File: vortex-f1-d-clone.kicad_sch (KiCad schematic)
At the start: 60 parts, among them IC1 74LS136, IC10 uPD765AC, IC11 74LS01, IC12 74LS38, IC13 74LS07, IC14 74LS139, IC2 74LS74, IC3 74LS85, IC4 27128, IC5 74LS14, IC6 74LS08, IC7 74LS25, IC8 74LS32, IC9 FDC_9229

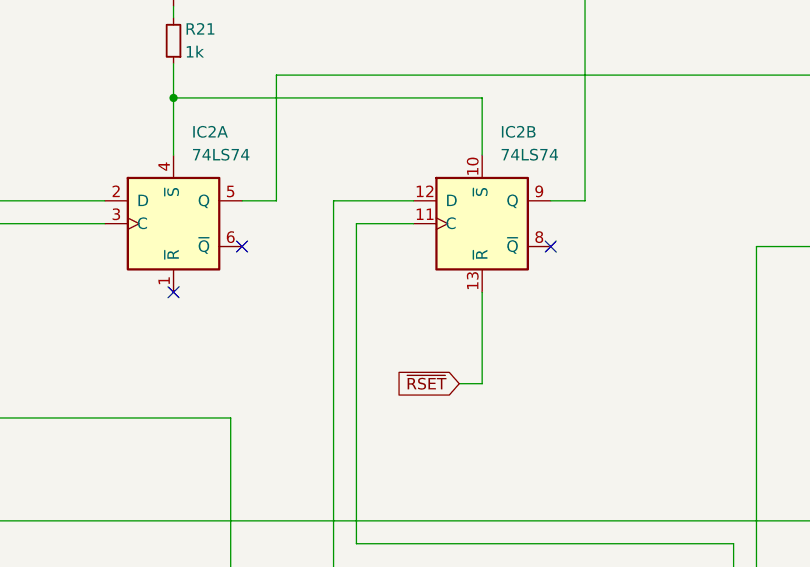
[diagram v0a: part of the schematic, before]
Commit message: Layout with ROM redone
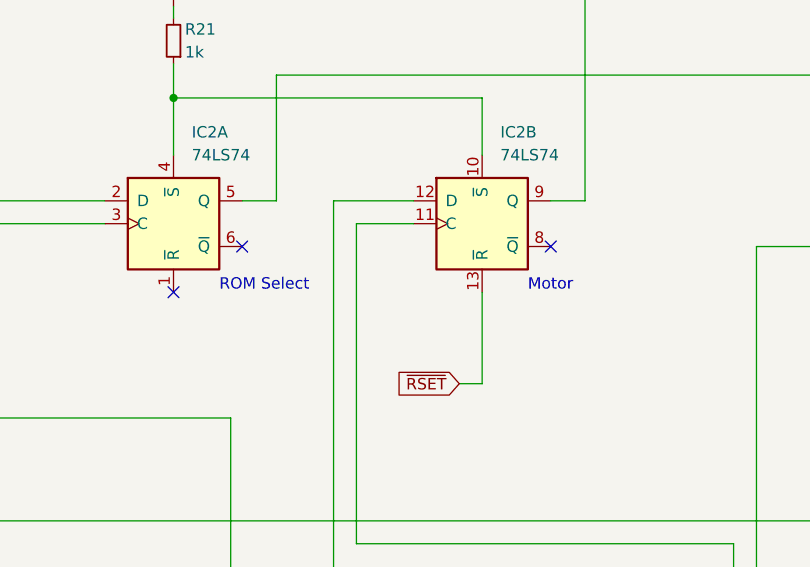
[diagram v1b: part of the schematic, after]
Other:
- note added: "Motor"
- note added: "ROM Select"
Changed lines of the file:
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@@
     (stroke (width 0) (type default) (color 0 0 0 0))
+  )
+  (text "Motor" (at 102.87 160.02 0)
+    (effects (font (size 1.27 1.27)) (justify left bottom))
+  )
+  (text "ROM Select\n" (at 68.58 160.02 0)
+    (effects (font (size 1.27 1.27)) (justify left bottom))
   )
   (label "D3" (at 63.5 297.18 0)

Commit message: sent TTL variant to aisler for production
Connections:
- net ~{IOWR}: now reaches IC10.3 (~{WR}), IC7.13, IC8.11, IC8.9
- net ~{FDCCS}: now reaches IC10.4 (~{CS}), IC14.5 (O1)
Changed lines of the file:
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@@
     (effects (font (size 1.27 1.27)) (justify right bottom))
+  )
+  (label "~{FDCCS}" (at 275.59 227.33 0)
+    (effects (font (size 1.27 1.27)) (justify left bottom))
+  )
+  (label "~{IOWR}" (at 107.315 269.24 0)
+    (effects (font (size 1.27 1.27)) (justify left bottom))
   )
   (label "CURSOR" (at 109.22 290.83 180)
